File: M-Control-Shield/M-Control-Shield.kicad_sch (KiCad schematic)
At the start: 26 parts, among them J1 Conn_01x08, J2 Conn_01x06, J3 Conn_01x10, J4 Conn_01x08

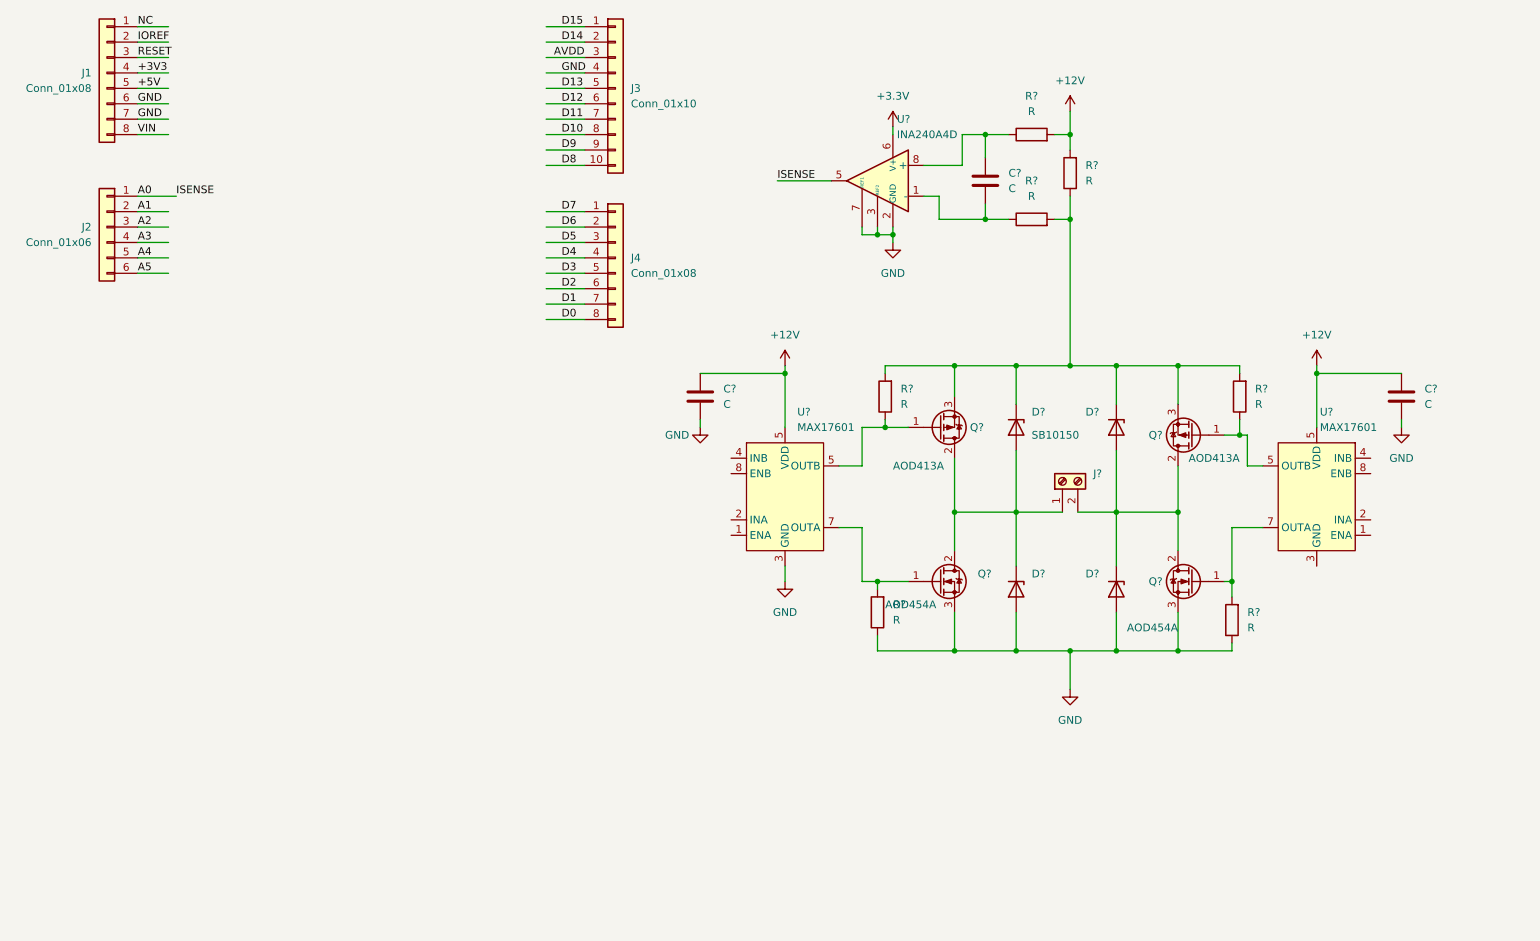
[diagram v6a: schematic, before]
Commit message: Adding connections for PWM and enables
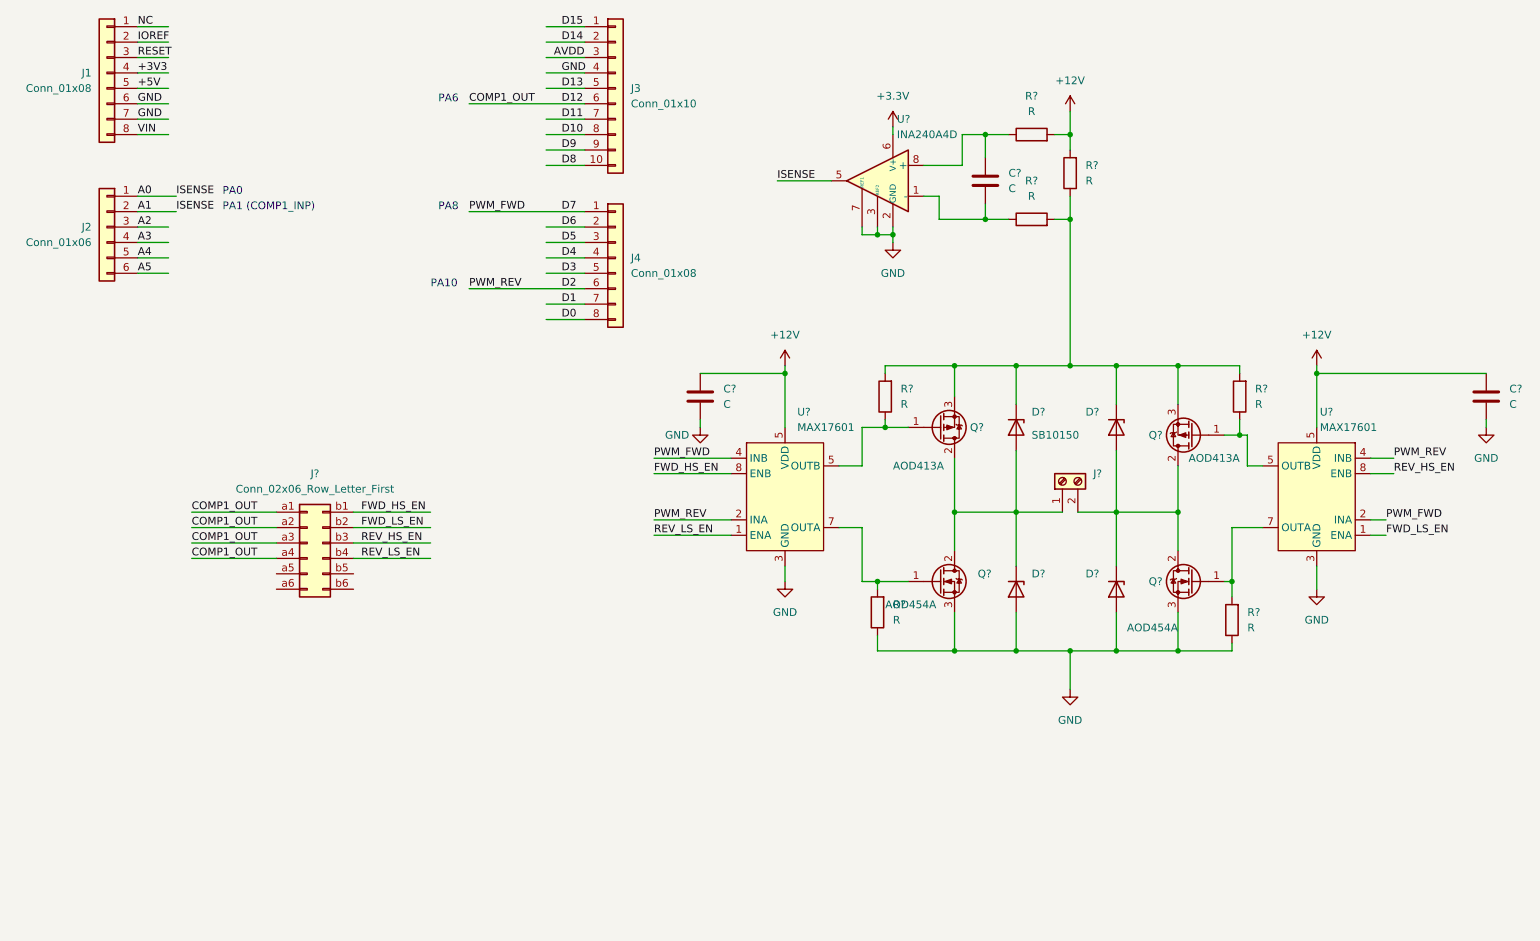
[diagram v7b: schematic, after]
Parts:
- added J?: Conn_02x06_Row_Letter_First, symbol Connector_Generic:Conn_02x06_Row_Letter_First
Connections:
- net A1 is gone; now on net A0: J2.2 (Pin_2)
- net D2: now also U?.2 (INA), U?.4 (INB)
- net D7: now also U?.2 (INA), U?.4 (INB)
- net GND: now also U?.3 (GND)
- net FWD_LS_EN: now reaches U?.1 (ENA)
- net FWD_LS_EN: now also J?.b2 (Pin_b2)
- net REV_HS_EN: now reaches U?.8 (ENB)
- net REV_HS_EN: now also J?.b3 (Pin_b3)
- net REV_LS_EN: now reaches U?.1 (ENA)
- net REV_LS_EN: now also J?.b4 (Pin_b4)
- net FWD_HS_EN: now reaches U?.8 (ENB)
- net FWD_HS_EN: now also J?.b1 (Pin_b1)
- net D12 renamed COMP1_OUT
- net COMP1_OUT: now also J?.a1 (Pin_a1), J?.a2 (Pin_a2), J?.a3 (Pin_a3), J?.a4 (Pin_a4)
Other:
- note added: "PA0"
- note added: "PA1 (COMP1_INP)"
- note added: "PA10"
- note added: "PA6"
- note added: "PA8"
- moved on the sheet: C?

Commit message: Added safety latch for shoot through
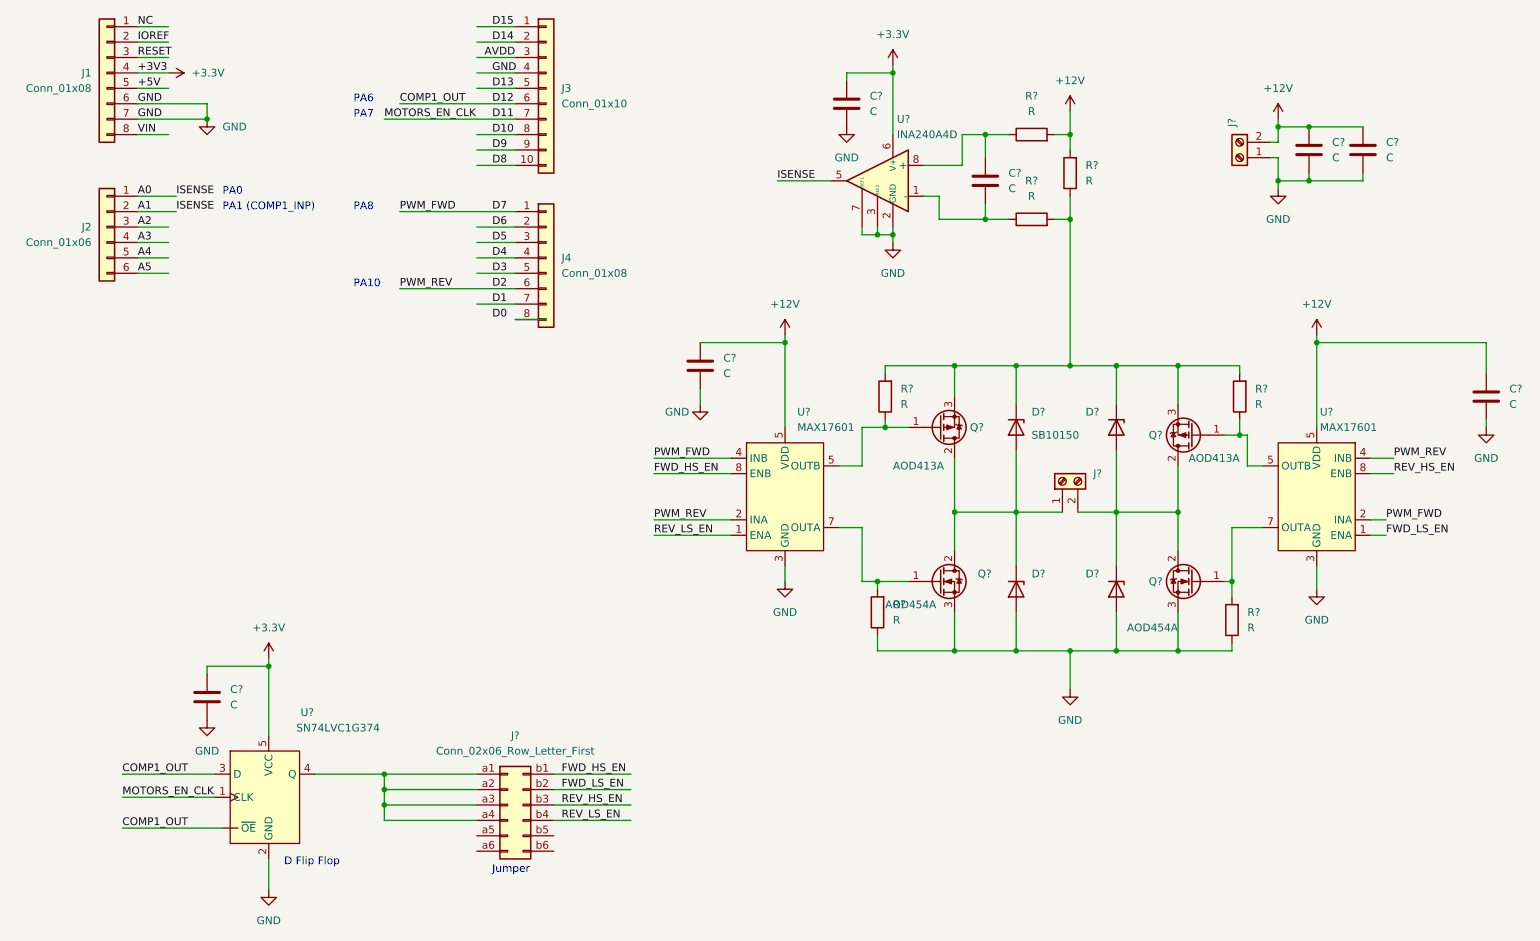
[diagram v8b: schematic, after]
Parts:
- added C? (x4): C, Capacitor_SMD:C_0603_1608Metric, symbol Device:C
- added J?: Screw_Terminal_01x02, TerminalBlock_Phoenix:TerminalBlock_Phoenix_PT-1,5-2-5.0-H_1x02_P5.00mm_Horizontal, symbol Connector:Screw_Terminal_01x02
- added U?: SN74LVC1G374, Package_TO_SOT_SMD:SOT-23-6, symbol 74xx:SN74LVC1G374
- J?: footprint (none) -> Connector_PinHeader_1.27mm:PinHeader_2x06_P1.27mm_Vertical
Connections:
- net +3V3 is gone; now on net +3.3V: J1.4 (Pin_4)
- net +12V: now also C?.1, C?.1, J?.2 (Pin_2)
- net +3.3V: now also C?.1, C?.1, U?.5 (VCC)
- net COMP1_OUT: now also U?. (~{OE}), U?.3 (D); no longer J?.a1 (Pin_a1), J?.a2 (Pin_a2), J?.a3 (Pin_a3), J?.a4 (Pin_a4)
- net D0: no longer J4.8 (Pin_8)
- net D11: now also U?.1 (CLK)
- net GND: now also C?.2, C?.2, C?.2, C?.2, J?.1 (Pin_1), U?.2 (GND)
- new net: J?.a1 (Pin_a1), J?.a2 (Pin_a2), J?.a3 (Pin_a3), J?.a4 (Pin_a4), U?.4 (Q)
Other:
- note added: "D Flip Flop"
- note added: "Jumper"
- note added: "PA7"
- moved on the sheet: C?, J3, J4, J?
